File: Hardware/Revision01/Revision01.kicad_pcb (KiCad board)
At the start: 4 copper layers, 100 x 119.8 mm, 76 parts, among them J1 Battery connector, J2 StrainConn, J3 StrainConn, J4 StrainConn, J5 StrainConn, J6 StrainConn, J7 StrainConn, J8 StrainConn, J9 StrainConn, Q3 NMOS, Q4 PMOS, Q6 PMOS, SW2 SW_SPST_LED, U10 NCP1117LPST50T3G, U11 LP5813BDRRR, U2 MRF89XAM9AT-I/RM, U3 NUCLEO-L476RG, U4 ICM-45605

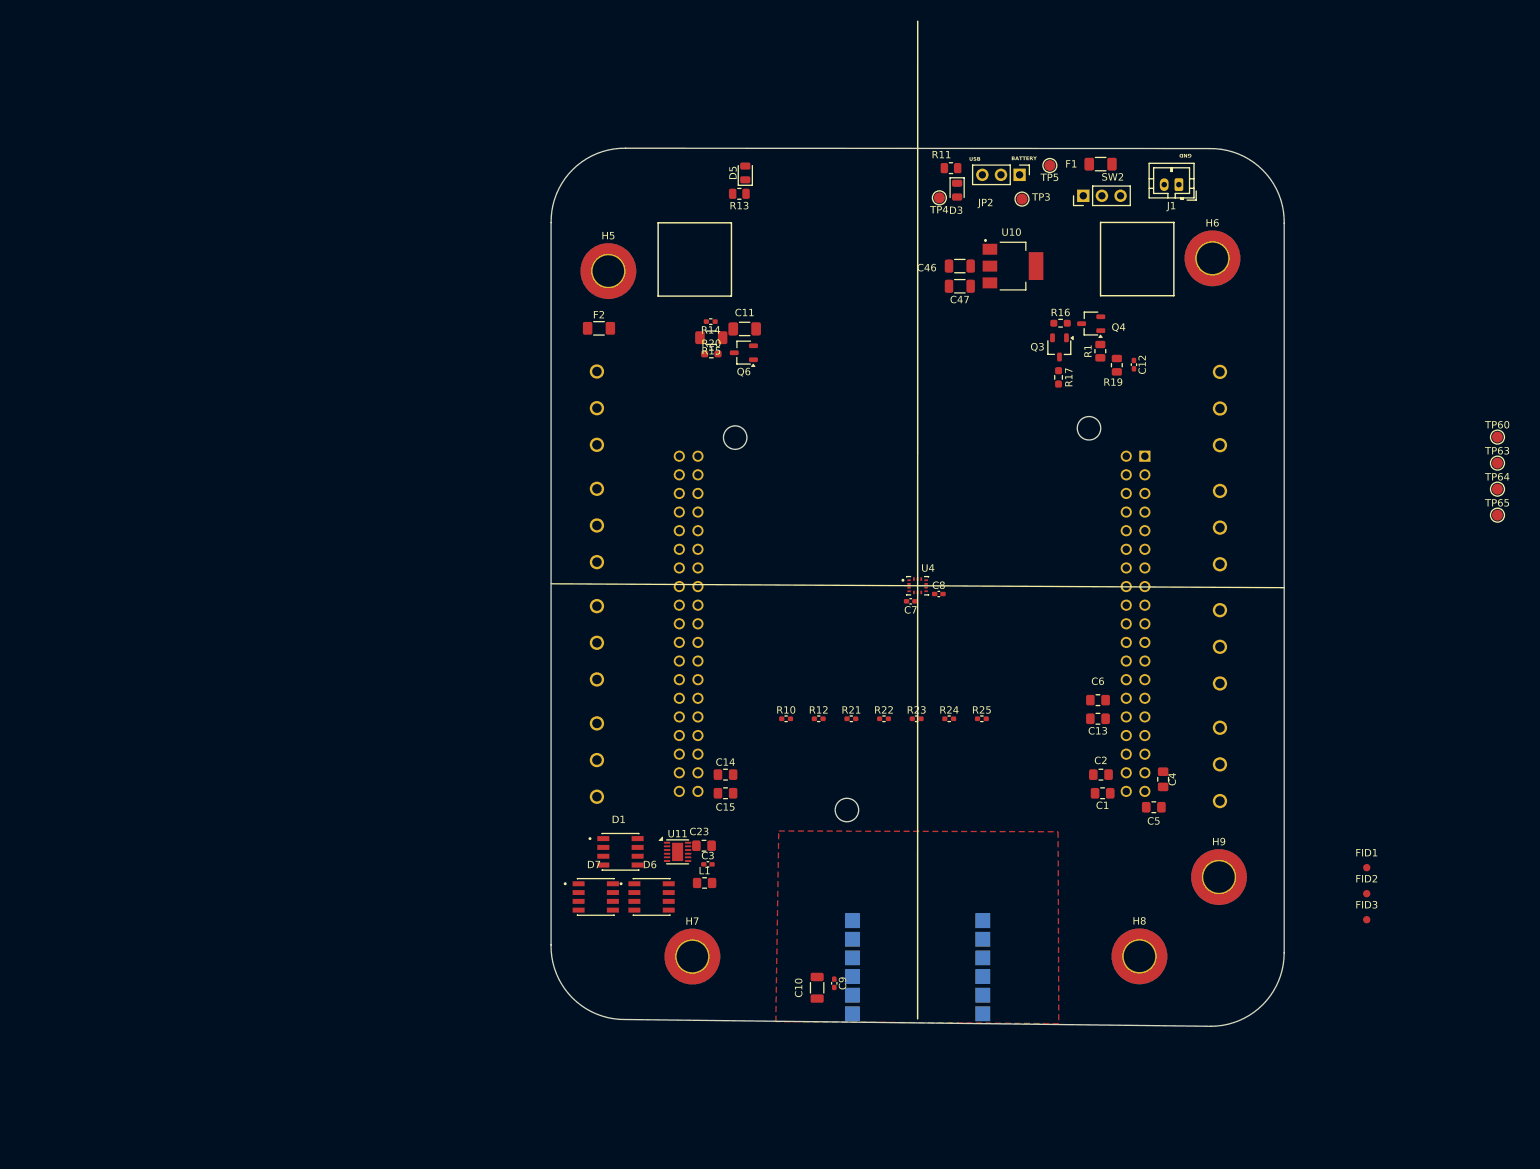
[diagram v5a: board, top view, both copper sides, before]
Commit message: branch fuses selected. Ready for PCB layout
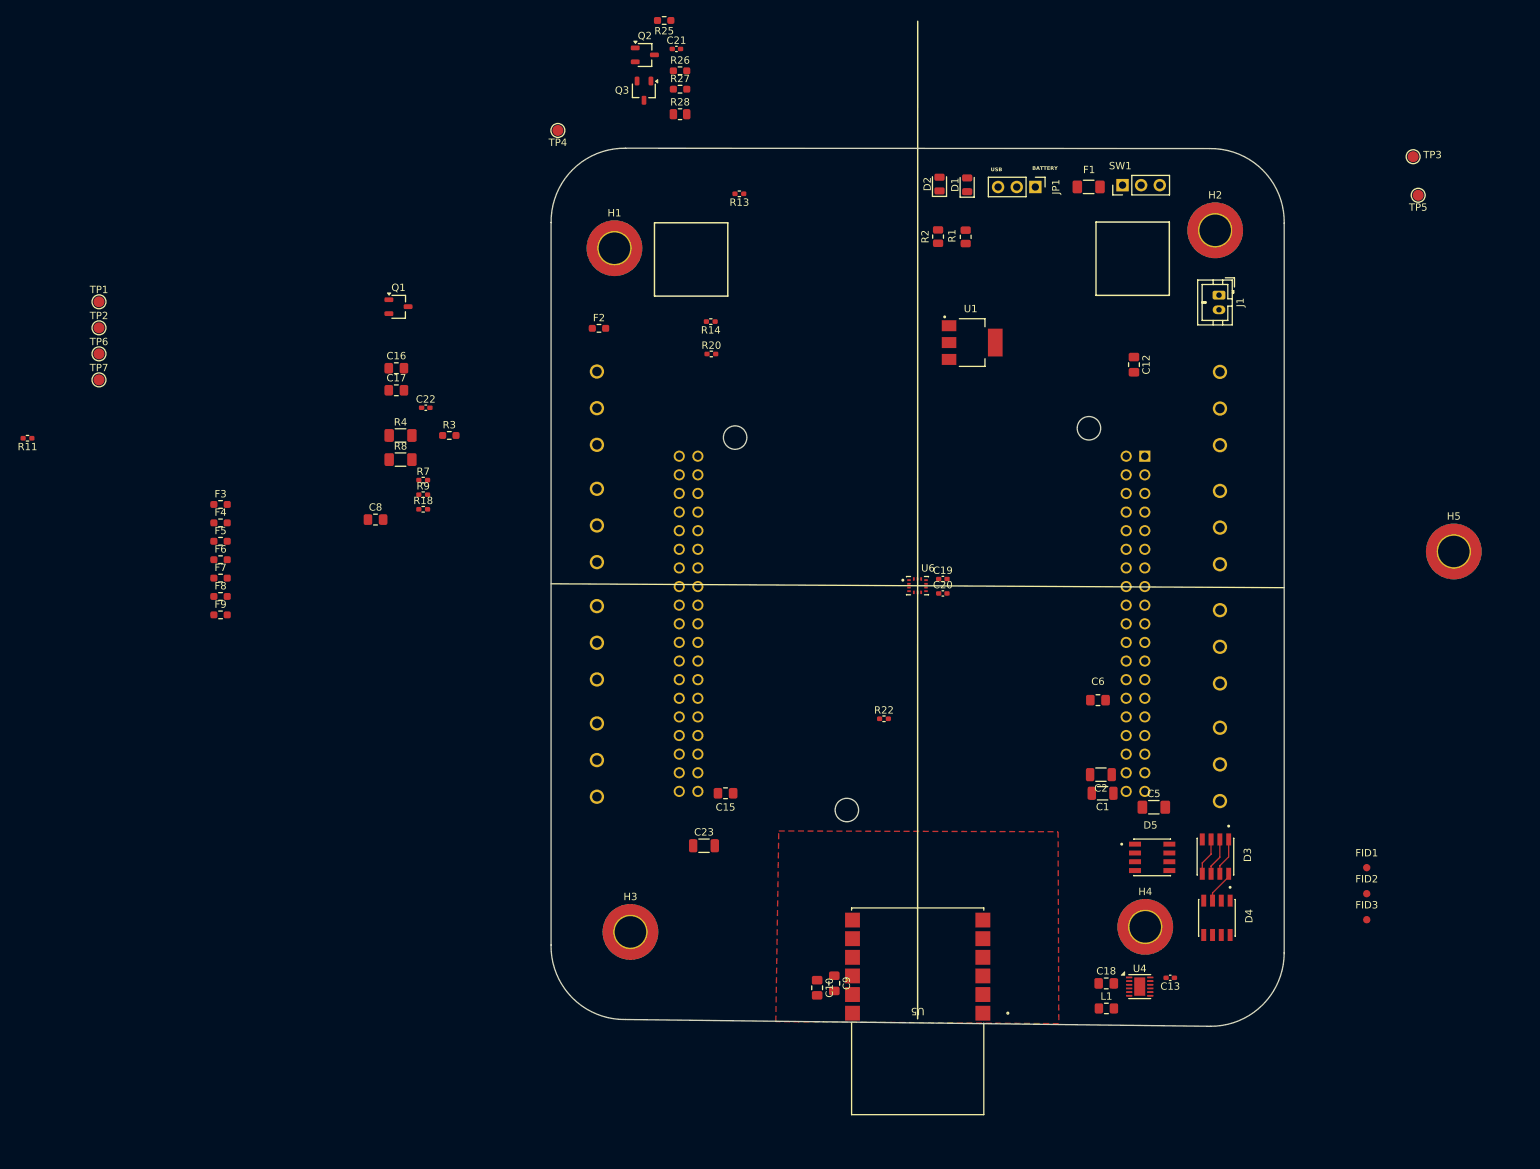
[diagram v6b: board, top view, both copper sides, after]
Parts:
- removed C11: 100uF, Capacitor_SMD:C_1206_3216Metric_Pad1.33x1.80mm_HandSolder
- removed C14, C4: 10nF, Capacitor_SMD:C_0805_2012Metric_Pad1.18x1.45mm_HandSolder
- removed C3: 10uF, Capacitor_SMD:C_0402_1005Metric_Pad0.74x0.62mm_HandSolder
- removed C46, C47: 10uF, Capacitor_SMD:C_1206_3216Metric
- removed C7: 0.1uF, Capacitor_SMD:C_0402_1005Metric_Pad0.74x0.62mm_HandSolder
- removed D6, D7: RGBW_LED, RGBW:SOL120P540X160-8N
- removed H6, H7, H8, H9: MountingHole_Pad_MP, MountingHole:MountingHole_4.3mm_M4_ISO7380_Pad_TopBottom
- removed JP2: Jumper_3_Bridged12, Connector_PinHeader_2.54mm:PinHeader_1x03_P2.54mm_Vertical
- removed Q4, Q6: PMOS, Package_TO_SOT_SMD:TSOT-23
- removed R10, R12, R21, R23, R24: 1.6K +-1%, Resistor_SMD:R_0402_1005Metric_Pad0.72x0.64mm_HandSolder
- removed R15: 0K +-1%, Resistor_SMD:R_1206_3216Metric_Pad1.30x1.75mm_HandSolder
- removed R16, R17: 10K +-1%, Resistor_SMD:R_0603_1608Metric_Pad0.98x0.95mm_HandSolder
- removed R19: 3.3K +-1%, Resistor_SMD:R_0805_2012Metric
- removed SW2: SW_SPST_LED, Connector_PinHeader_2.54mm:PinHeader_1x03_P2.54mm_Vertical
- removed TP60, TP63, TP64, TP65: TestPoint, TestPoint:TestPoint_Pad_D1.5mm
- removed U10: NCP1117LPST50T3G, NCP1117LPST50T3G:SOT230P700X180-4N
- removed U11: LP5813BDRRR, Package_SON:WSON-12-1EP_3x3mm_P0.5mm_EP1.5x2.5mm
- removed U3: NUCLEO-L476RG, NUCLEO-L476RG:MODULE_NUCLEO-L476RG
- added C16: 10nF, Capacitor_SMD:C_0805_2012Metric_Pad1.18x1.45mm_HandSolder, F.Cu at (89.9, 63.0)
- added C17: 10nF, Capacitor_SMD:C_0805_2012Metric_Pad1.18x1.45mm_HandSolder, F.Cu at (89.9, 66.0)
- added C18: 22uF, Capacitor_SMD:C_0805_2012Metric_Pad1.18x1.45mm_HandSolder, F.Cu at (186.7, 146.9)
- added C19: 0.1uF, Capacitor_SMD:C_0402_1005Metric_Pad0.74x0.62mm_HandSolder, F.Cu at (164.5, 91.7)
- added C20: 0.1uF, Capacitor_SMD:C_0402_1005Metric_Pad0.74x0.62mm_HandSolder, F.Cu at (164.5, 93.7)
- added C21: 0.1uF, Capacitor_SMD:C_0402_1005Metric_Pad0.74x0.62mm_HandSolder, F.Cu at (128.1, 19.4)
- added C22: 0.1uF, Capacitor_SMD:C_0402_1005Metric_Pad0.74x0.62mm_HandSolder, F.Cu at (93.9, 68.3)
- added D2: RED LED, LED_SMD:LED_0805_2012Metric, F.Cu at (164.0, 37.8)
- added D4: RGBW_LED, RGBW:SOL120P540X160-8N, F.Cu at (201.8, 137.9)
- added F3: Polyfuse_Small, Resistor_SMD:R_0603_1608Metric_Pad0.98x0.95mm_HandSolder, F.Cu at (65.9, 81.5)
- added F4: Polyfuse_Small, Resistor_SMD:R_0603_1608Metric_Pad0.98x0.95mm_HandSolder, F.Cu at (65.9, 84.1)
- added F5: Polyfuse_Small, Resistor_SMD:R_0603_1608Metric_Pad0.98x0.95mm_HandSolder, F.Cu at (65.9, 86.6)
- added F6: Polyfuse_Small, Resistor_SMD:R_0603_1608Metric_Pad0.98x0.95mm_HandSolder, F.Cu at (65.9, 89.1)
- added F7: Polyfuse_Small, Resistor_SMD:R_0603_1608Metric_Pad0.98x0.95mm_HandSolder, F.Cu at (65.9, 91.6)
- added F8: Polyfuse_Small, Resistor_SMD:R_0603_1608Metric_Pad0.98x0.95mm_HandSolder, F.Cu at (65.9, 94.1)
- added F9: Polyfuse_Small, Resistor_SMD:R_0603_1608Metric_Pad0.98x0.95mm_HandSolder, F.Cu at (65.9, 96.6)
- added H1: MountingHole_Pad_MP, MountingHole:MountingHole_4.3mm_M4_ISO7380_Pad_TopBottom, F.Cu at (119.7, 46.6)
- added H2: MountingHole_Pad_MP, MountingHole:MountingHole_4.3mm_M4_ISO7380_Pad_TopBottom, F.Cu at (201.6, 44.1)
- added H3: MountingHole_Pad_MP, MountingHole:MountingHole_4.3mm_M4_ISO7380_Pad_TopBottom, F.Cu at (121.8, 139.8)
- added H4: MountingHole_Pad_MP, MountingHole:MountingHole_4.3mm_M4_ISO7380_Pad_TopBottom, F.Cu at (192.1, 139.2)
- added JP1: Jumper_3_Bridged12, Connector_PinHeader_2.54mm:PinHeader_1x03_P2.54mm_Vertical, F.Cu at (177.1, 38.2)
- added Q1: PMOS, Package_TO_SOT_SMD:TSOT-23, F.Cu at (90.2, 54.6)
- added Q2: NMOS, Package_TO_SOT_SMD:TSOT-23, F.Cu at (123.8, 20.2)
- added R18: 1.6K +-1%, Resistor_SMD:R_0402_1005Metric_Pad0.72x0.64mm_HandSolder, F.Cu at (93.6, 82.2)
- added R2: 330 +-5%, Resistor_SMD:R_0805_2012Metric, F.Cu at (163.8, 45.0)
- added R26: 10K +-1%, Resistor_SMD:R_0603_1608Metric_Pad0.98x0.95mm_HandSolder, F.Cu at (128.6, 22.4)
- added R27: 15K +-1%, Resistor_SMD:R_0603_1608Metric_Pad0.98x0.95mm_HandSolder, F.Cu at (128.6, 24.9)
- added R28: 3.3K +-1%, Resistor_SMD:R_0805_2012Metric, F.Cu at (128.6, 28.3)
- added R3: 10K +-1%, Resistor_SMD:R_0603_1608Metric_Pad0.98x0.95mm_HandSolder, F.Cu at (97.1, 72.1)
- added R4: 0K +-1%, Resistor_SMD:R_1206_3216Metric_Pad1.30x1.75mm_HandSolder, F.Cu at (90.5, 72.1)
- added R7: 1.6K +-1%, Resistor_SMD:R_0402_1005Metric_Pad0.72x0.64mm_HandSolder, F.Cu at (93.6, 78.2)
- added R8: 0K +-1%, Resistor_SMD:R_1206_3216Metric_Pad1.30x1.75mm_HandSolder, F.Cu at (90.5, 75.4)
- added R9: 1.6K +-1%, Resistor_SMD:R_0402_1005Metric_Pad0.72x0.64mm_HandSolder, F.Cu at (93.6, 80.2)
- added SW1: SW_SPST_LED, Connector_PinHeader_2.54mm:PinHeader_1x03_P2.54mm_Vertical, F.Cu at (189.0, 38.0)
- added TP1: TestPoint, TestPoint:TestPoint_Pad_D1.5mm, F.Cu at (49.4, 53.9)
- added TP2: TestPoint, TestPoint:TestPoint_Pad_D1.5mm, F.Cu at (49.4, 57.5)
- added TP6: TestPoint, TestPoint:TestPoint_Pad_D1.5mm, F.Cu at (49.4, 61.0)
- added TP7: TestPoint, TestPoint:TestPoint_Pad_D1.5mm, F.Cu at (49.4, 64.5)
- added U1: NCP1117LPST50T3G, NCP1117LPST50T3G:SOT230P700X180-4N, F.Cu at (168.5, 59.5)
- added U5: MRF89XAM9AT-I/RM, MRF89XAM9AT-antenna:MOD_MRF89XAM9A_MCH, F.Cu at (161.0, 150.7)
- added U6: ICM-45605, ICM-45605-gyroscope:XDCR_ICM-45605, F.Cu at (161.0, 92.6)
- C1, C2: value 10nF -> 10uF; footprint Capacitor_SMD:C_0805_2012Metric_Pad1.18x1.45mm_HandSolder -> Capacitor_SMD:C_1206_3216Metric
- C10: value 10uF -> 10nF; footprint Capacitor_SMD:C_1206_3216Metric -> Capacitor_SMD:C_0805_2012Metric_Pad1.18x1.45mm_HandSolder
- C12, C8, C9: value 0.1uF -> 10nF; footprint Capacitor_SMD:C_0402_1005Metric_Pad0.74x0.62mm_HandSolder -> Capacitor_SMD:C_0805_2012Metric_Pad1.18x1.45mm_HandSolder
- C13: value 10nF -> 10uF; footprint Capacitor_SMD:C_0805_2012Metric_Pad1.18x1.45mm_HandSolder -> Capacitor_SMD:C_0402_1005Metric_Pad0.74x0.62mm_HandSolder
- C23: value 22uF -> 10uF; footprint Capacitor_SMD:C_0805_2012Metric_Pad1.18x1.45mm_HandSolder -> Capacitor_SMD:C_1206_3216Metric
- C5: value 10nF -> 100uF; footprint Capacitor_SMD:C_0805_2012Metric_Pad1.18x1.45mm_HandSolder -> Capacitor_SMD:C_1206_3216Metric_Pad1.33x1.80mm_HandSolder
- D1: value RGBW_LED -> BLUE LED; footprint RGBW:SOL120P540X160-8N -> LED_SMD:LED_0805_2012Metric
- D3: value BLUE LED -> RGBW_LED; footprint LED_SMD:LED_0805_2012Metric -> RGBW:SOL120P540X160-8N
- D5: value RED LED -> RGBW_LED; footprint LED_SMD:LED_0805_2012Metric -> RGBW:SOL120P540X160-8N
- F2: value Polyfuse -> Polyfuse_Small; footprint Resistor_SMD:R_1206_3216Metric_Pad1.30x1.75mm_HandSolder -> Resistor_SMD:R_0603_1608Metric_Pad0.98x0.95mm_HandSolder
- Q3: value NMOS -> PMOS
- R1: value 15K +-1% -> 330 +-5%
- R11, R13: value 330 +-5% -> 1.6K +-1%; footprint Resistor_SMD:R_0805_2012Metric -> Resistor_SMD:R_0402_1005Metric_Pad0.72x0.64mm_HandSolder
- R20: value 10K +-1% -> 1.6K +-1%; footprint Resistor_SMD:R_0603_1608Metric_Pad0.98x0.95mm_HandSolder -> Resistor_SMD:R_0402_1005Metric_Pad0.72x0.64mm_HandSolder
- R25: value 1.6K +-1% -> 10K +-1%; footprint Resistor_SMD:R_0402_1005Metric_Pad0.72x0.64mm_HandSolder -> Resistor_SMD:R_0603_1608Metric_Pad0.98x0.95mm_HandSolder
- U2: value MRF89XAM9AT-I/RM -> NUCLEO-L476RG; footprint MRF89XAM9AT-antenna:MOD_MRF89XAM9A_MCH -> NUCLEO-L476RG:MODULE_NUCLEO-L476RG
- U4: value ICM-45605 -> LP5813BDRRR; footprint ICM-45605:XDCR_ICM-45605 -> Package_SON:WSON-12-1EP_3x3mm_P0.5mm_EP1.5x2.5mm
- moved R11 131.2 mm to (39.6, 72.5)
- moved H5 121.5 mm to (234.2, 88.0)
- moved D5 108.6 mm to (193.0, 129.7), turned to 0 degrees
- moved R25 104.6 mm to (126.5, 15.5), turned to 180 degrees
- moved D1 102.5 mm to (167.8, 37.9), turned to 90 degrees
- moved D3 97.5 mm to (201.6, 129.6)
- moved C8 77.5 mm to (87.1, 83.6)
- moved Q3 66.6 mm to (123.7, 25.1)
- moved U2 66.3 mm to (160.3, 84.5), turned to 180 degrees
- moved U4 62.5 mm to (191.3, 147.3)
- moved L1 57.4 mm to (186.8, 150.3)
- moved TP3 53.7 mm to (228.6, 34.1)
- moved TP4 52.8 mm to (112.0, 30.5)
- moved TP5 50.4 mm to (229.3, 39.4)
- moved C13 36.7 mm to (195.5, 146.1)
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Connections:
- C1 pad 1: /AIN_1 -> +V_batt
- C1 pad 2: GND -> Earth
- C10 pad 1: +3.3V -> /AIN_4
- C10 pad 2: GND -> Earth
- C12 pad 1: /BatteryV_AIN -> /AIN_5
- C12 pad 2: GND -> Earth
- C13 pad 1: /AIN_6 -> +3.3V
- C13 pad 2: GND -> Earth
- C15 pad 1: /AIN_8 -> /AIN_6
- C15 pad 2: GND -> Earth
- C2 pad 1: /AIN_2 -> +5V_External_LDO
- C2 pad 2: GND -> Earth
- C23 pad 1: Net-(U11-VOUT) -> +3.3V
- C23 pad 2: GND -> Earth
- C5 pad 1: /AIN_4 -> /Application/+StrainV
- C5 pad 2: GND -> Earth
- C6 pad 1: /AIN_5 -> /AIN_1
- C6 pad 2: GND -> Earth
- C8 pad 1: +3.3V -> /AIN_2
- C8 pad 2: GND -> Earth
- C9 pad 1: +3.3V -> /AIN_3
- C9 pad 2: GND -> Earth
- D1 pad 1: /Application/U1_OUT3 -> Net-(D1-K)
- D1 pad 2: /Application/U1_OUT0 -> +5V_USB
- D3 pad 1: Net-(D3-K) -> /Application/U1_OUT1
- D3 pad 2: +5V_USB -> /Application/U1_OUT2
- D5 pad 1: Net-(D5-K) -> /Application/U1_OUT3
- D5 pad 2: +3.3V -> /Application/U1_OUT0
- F2 pad 1: +5V -> /Application/+StrainV
- F2 pad 2: Net-(Q6-S) -> Net-(J2-Pin_3)
- J1 pad 1: GND -> Earth
- J2 pad 1: GND -> Earth
- J2 pad 3: /Application/+StrainV -> Net-(J2-Pin_3)
- J3 pad 1: GND -> Earth
- J3 pad 3: /Application/+StrainV -> Net-(J3-Pin_3)
- J4 pad 1: GND -> Earth
- J4 pad 3: /Application/+StrainV -> Net-(J4-Pin_3)
- J5 pad 1: GND -> Earth
- J5 pad 3: /Application/+StrainV -> Net-(J5-Pin_3)
- J6 pad 1: GND -> Earth
- J6 pad 3: /Application/+StrainV -> Net-(J6-Pin_3)
- J7 pad 1: GND -> Earth
- J7 pad 3: /Application/+StrainV -> Net-(J7-Pin_3)
- J8 pad 1: GND -> Earth
- J8 pad 3: /Application/+StrainV -> Net-(J8-Pin_3)
- J9 pad 1: GND -> Earth
- J9 pad 3: /Application/+StrainV -> Net-(J9-Pin_3)
- L1 pad 2: Net-(U11-SW) -> Net-(U4-SW)
- Q3 pad 2: /BatteryV_Div_Enable_GPIO -> Net-(Q2-D)
- Q3 pad 3: GND -> +V_batt
- R1 pad 1: /BatteryV_AIN -> Net-(D1-K)
- R1 pad 2: Net-(Q4-D) -> Earth
- R11 pad 1: Net-(D3-K) -> /Application/OpAmpOutput3
- R11 pad 2: GND -> /AIN_3
- R13 pad 1: Net-(D5-K) -> /Application/OpAmpOutput4
- R13 pad 2: GND -> /AIN_4
- R14 pad 1: /Application/OpAmpOutput3 -> /Application/OpAmpOutput5
- R14 pad 2: /AIN_3 -> /AIN_5
- R20 pad 1: /StrainV_Enable_GPIO -> /Application/OpAmpOutput7
- R20 pad 2: Net-(Q6-S) -> /AIN_7
- R22 pad 1: /Application/OpAmpOutput5 -> /Application/OpAmpOutput8
- R22 pad 2: /AIN_5 -> /AIN_8
- R25 pad 1: /Application/OpAmpOutput8 -> Earth
- R25 pad 2: /AIN_8 -> /BatteryV_Div_Enable_GPIO
- TP3 pad 1: +5V_External_LDO -> +V_batt
- TP4 pad 1: +5V_USB -> /PB3/JTDO-TRACESWO/TIM2_CH2/SPI1_SCK/SPI3_SCK/USART1_RTS_DE/COMP2_INM
- TP5 pad 1: +V_batt -> Net-(U2A-BOOT0)
- U4 pad 1: /PB14_SPI2_MISO -> Net-(U4-SW)
- U4 pad 10: unconnected-(U4-RESV_10-Pad10) -> /Application/U1_OUT0
- U4 pad 11: unconnected-(U4-RESV_11-Pad11) -> /LP5813_EN_GPIO
- U4 pad 12: /ICM_CS_GPIO -> +3.3V
- U4 pad 13: /PB13_SPI2_SCK -> Earth
- U4 pad 2: unconnected-(U4-RESV/MAS_DA-Pad2) -> Net-(U4-VOUT)
- U4 pad 3: unconnected-(U4-RESV/MAS_CLK-Pad3) -> Earth
- U4 pad 4: /ICM_INT1_GPIO -> unconnected-(U4-SYNC-Pad4)
- U4 pad 5: +3.3V -> /I2C_SCL
- U4 pad 6: GND -> /I2C_SDA
- U4 pad 7: unconnected-(U4-RESV_7-Pad7) -> /Application/U1_OUT3
- U4 pad 8: +3.3V -> /Application/U1_OUT2
- U4 pad 9: /ICM_INT2_GPIO -> /Application/U1_OUT1
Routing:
- net /Application/U1_OUT2: track 0.00 -> 5.18 mm
- net /Application/U1_OUT3: track 0.00 -> 5.18 mm
- net /Application/U1_OUT1: track 0.00 -> 5.18 mm
- net /Application/U1_OUT0: track 0.00 -> 4.88 mm
- added copper zone on F.Cu, net /I2C_SDA
- added copper zone on In1.Cu, net Earth
- added copper zone on In2.Cu, net Earth
- removed copper zone on F.Cu, net GND
- removed copper zone on In1.Cu, net GND
- removed copper zone on In2.Cu, net GND
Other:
- board text removed: "GND"
